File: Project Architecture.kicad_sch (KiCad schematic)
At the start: 0 parts

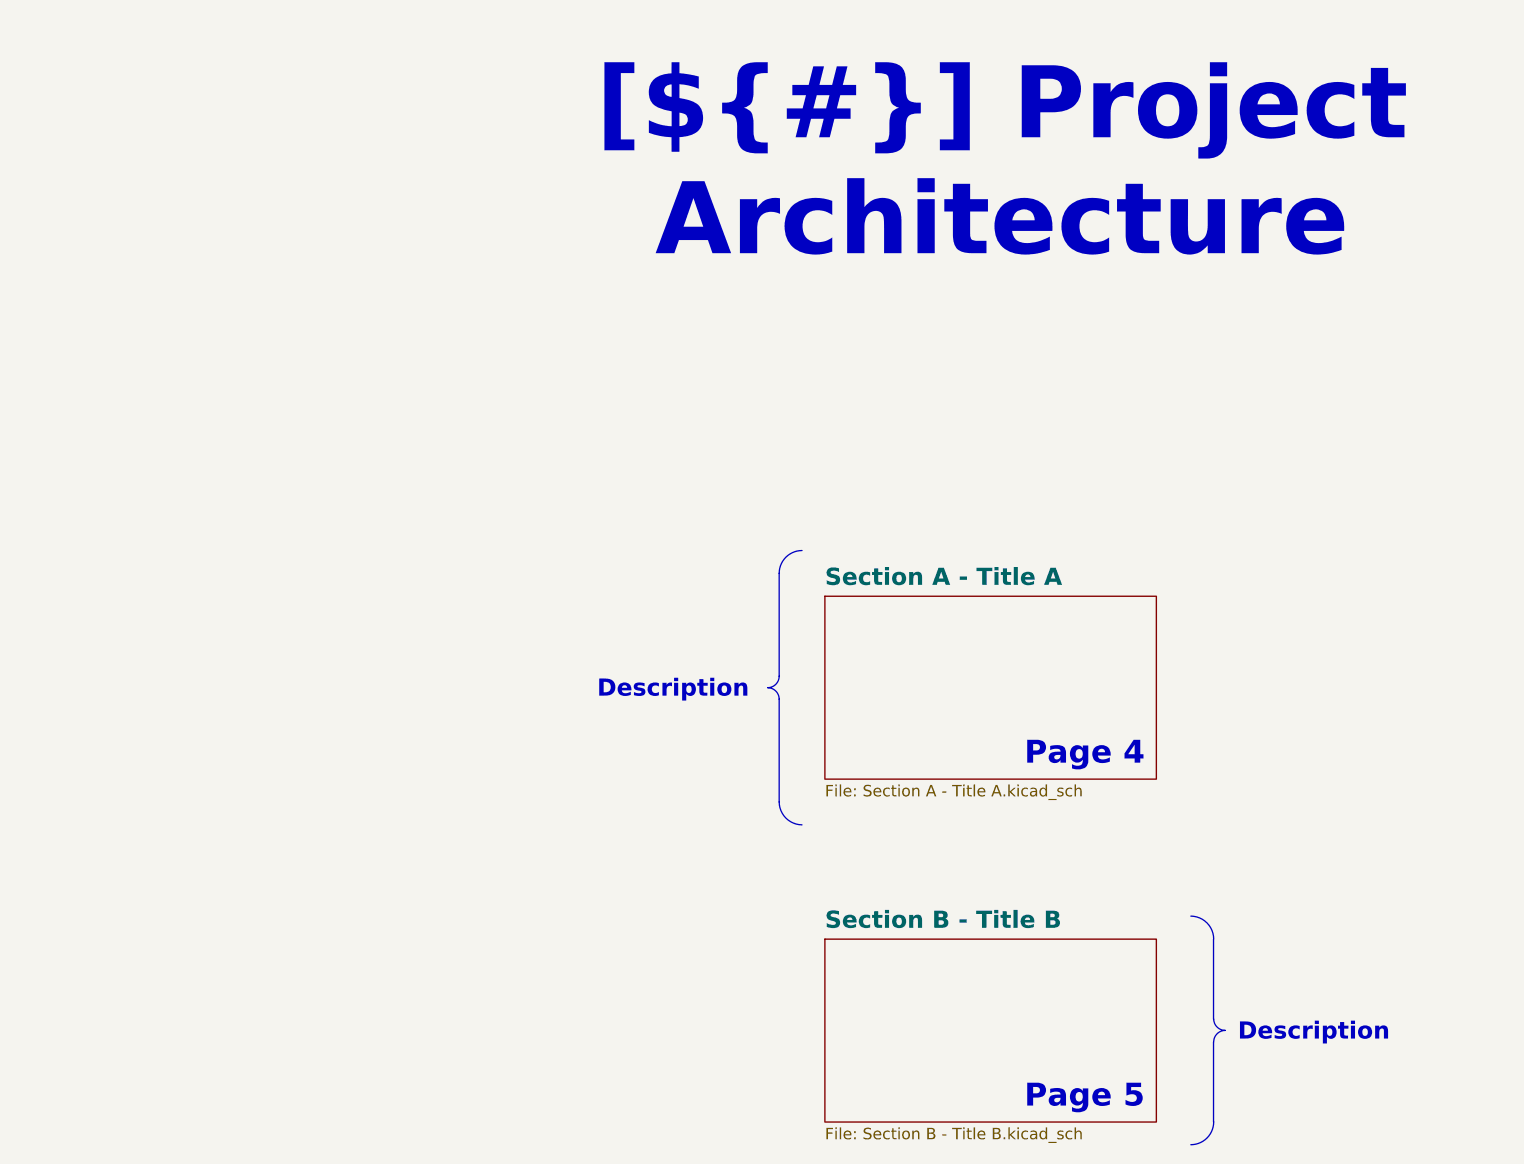
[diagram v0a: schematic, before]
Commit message: PCB[Layout and Routing]: Routing and layout done, changed to micofit connector, need to review and fix drc errors. SCH[Connector & Fuse]: Schmatic for connector, fuse and board to board layout, need to cleanup and add board standoffs.
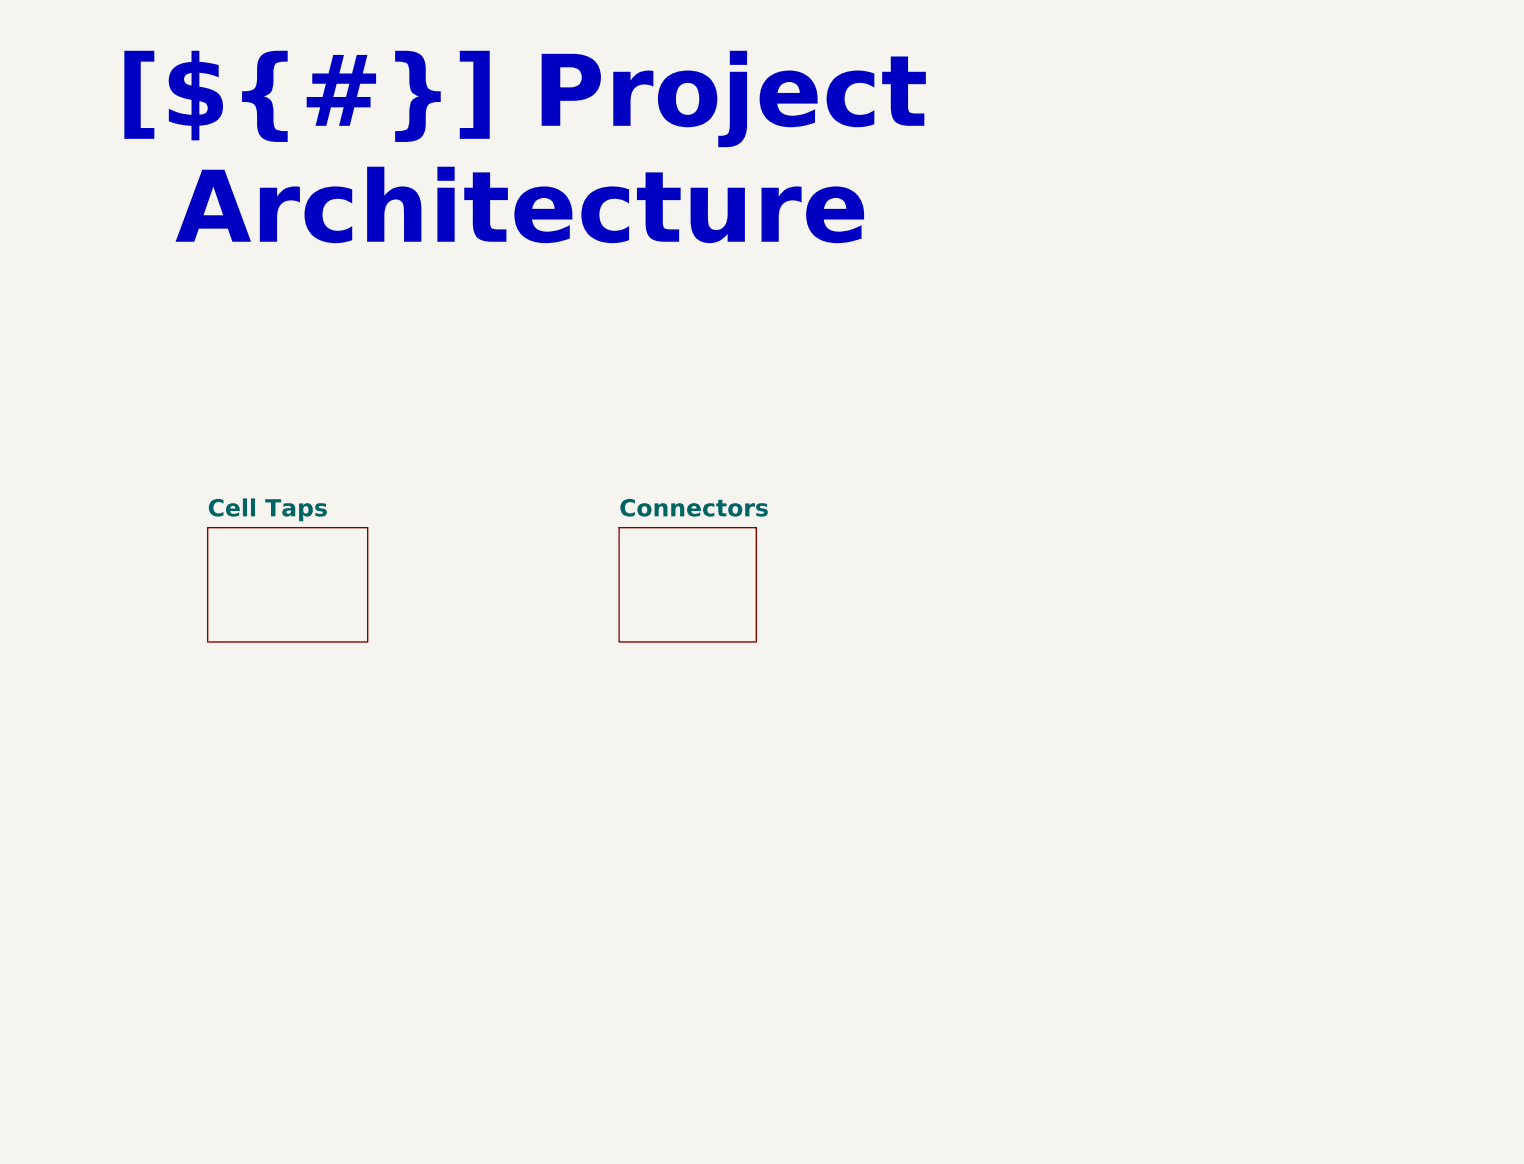
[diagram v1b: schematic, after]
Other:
- removed sheet Section A - Title A
- removed sheet Section B - Title B
- added sheet Cell Taps (celltaps.kicad_sch)
- added sheet Connectors (connectors.kicad_sch)
- note removed: "Page 4"
- note removed: "Page 5"

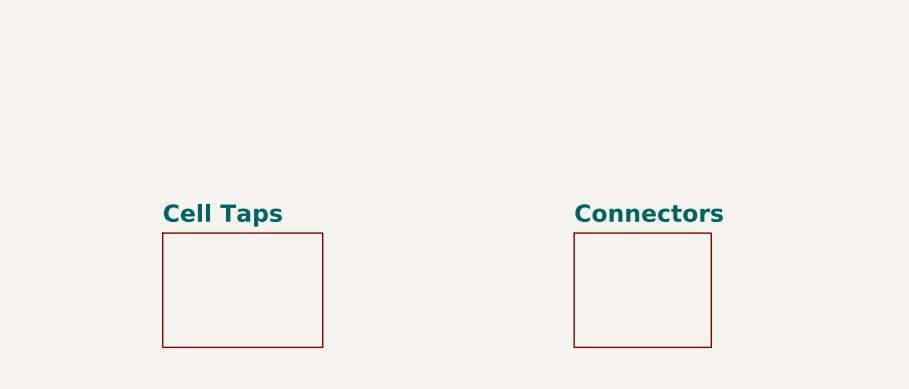
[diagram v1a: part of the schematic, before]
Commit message: PCB[Mounting]: Added standoffs going to test clearnaces. SCH[Mechanical]: Added standoffs, 14mm metal smt, small naming changes to match bms_slave sch.
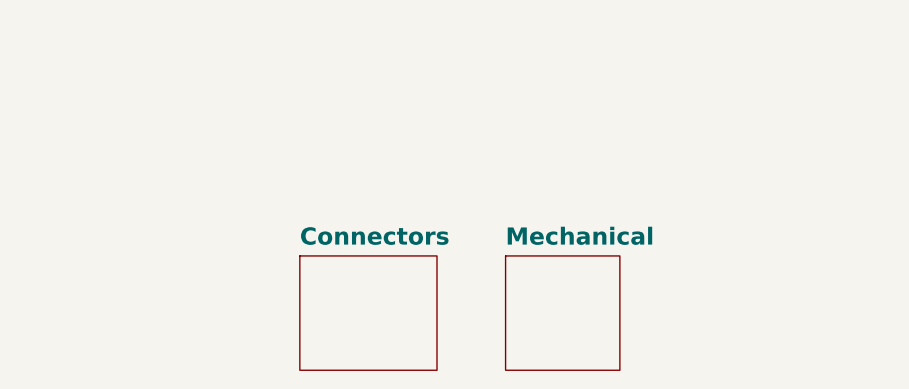
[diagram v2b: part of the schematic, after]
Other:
- removed sheet Cell Taps
- added sheet Mechanical (mechanical.kicad_sch)
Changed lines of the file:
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@@
 	(title_block
 		(title "Project Architecture")
-		(date "2026-10-12")
+		(date "2026-10-16")
 		(rev "${REVISION}")
 		(company "${COMPANY}")
@@
 	)
 	(sheet
-		(at 167.64 68.58)
+		(at 160.02 71.12)
+		(size 12.7 12.7)
+		(exclude_from_sim no)
+		(in_bom yes)
+		(on_board yes)
+		(dnp no)
+		(fields_autoplaced yes)
+		(stroke
+			(width 0.1524)
+			(type solid)
+		)
+		(fill
+			(color 0 0 0 0)
+		)
+		(property "Sheetname" "Mechanical"
+			(at 160.02 70.0909 0)
+			(show_name no)
+			(do_not_autoplace no)
+			(effects
+				(font
+					(size 1.905 1.905)
+					(thickness 0.381)
+					(bold yes)
+				)
+				(justify left bottom)
+			)
+		)
+		(property "Sheetfile" "mechanical.kicad_sch"
+			(at 160.02 84.4046 0)
+			(hide yes)
+			(show_name no)
+			(do_not_autoplace no)
+			(effects
+				(font
+					(size 1.27 1.27)
+				)
+				(justify left top)
+			)
+		)
+		(instances
+			(project "battery_interface_board"
+				(path "/f9e05184-c88b-4a88-ae9c-ab2bdb32be7c/c5103ceb-5325-4a84-a025-9638a412984e"
+					(page "5")
+				)
+			)
+		)
+	)
+	(sheet
+		(at 137.16 71.12)
 		(size 15.24 12.7)
 		(exclude_from_sim no)
@@
 		)
 		(property "Sheetname" "Connectors"
-			(at 167.64 67.5509 0)
+			(at 137.16 70.0909 0)
 			(show_name no)
 			(do_not_autoplace no)
@@
 		)
 		(property "Sheetfile" "connectors.kicad_sch"
-			(at 167.64 81.8646 0)
+			(at 137.16 84.4046 0)
 			(hide yes)
 			(show_name no)
@@
 				)
 			)
-		)
-	)
-	(sheet
-		(at 121.92 68.58)
-		(size 17.78 12.7)
-		(exclude_from_sim no)
-		(in_bom yes)
-		(on_board yes)
-		(dnp no)
-		(fields_autoplaced yes)
-		(stroke
-			(width 0.1524)
-			(type solid)
-		)
-		(fill
-			(color 0 0 0 0)
-		)
-		(property "Sheetname" "Cell Taps"
-			(at 121.92 67.5509 0)
-			(show_name no)
-			(do_not_autoplace no)
-			(effects
-				(font
-					(size 1.905 1.905)
-					(thickness 0.381)
-					(bold yes)
-				)
-				(justify left bottom)
-			)
-		)
-		(property "Sheetfile" "celltaps.kicad_sch"
-			(at 121.92 81.8646 0)
-			(hide yes)
-			(show_name no)
-			(do_not_autoplace no)
-			(effects
-				(font
-					(size 1.27 1.27)
-				)
-				(justify left top)
-			)
-		)
-		(instances
-			(project "battery_interface_board"
-				(path "/f9e05184-c88b-4a88-ae9c-ab2bdb32be7c/c5103ceb-5325-4a84-a025-9638a412984e"
-					(page "5")
-				)
-			)

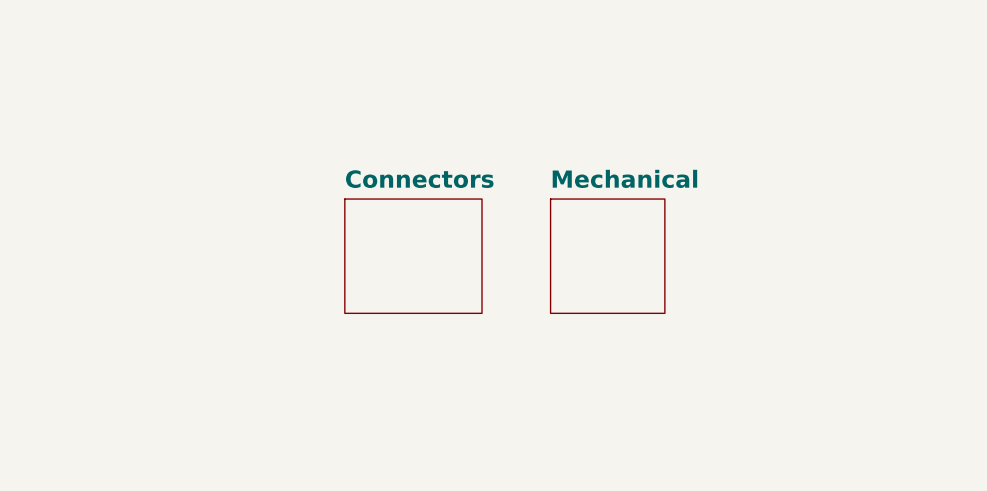
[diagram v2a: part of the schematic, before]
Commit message: SCH[Clean]: Cleaned up some schmatic errors.
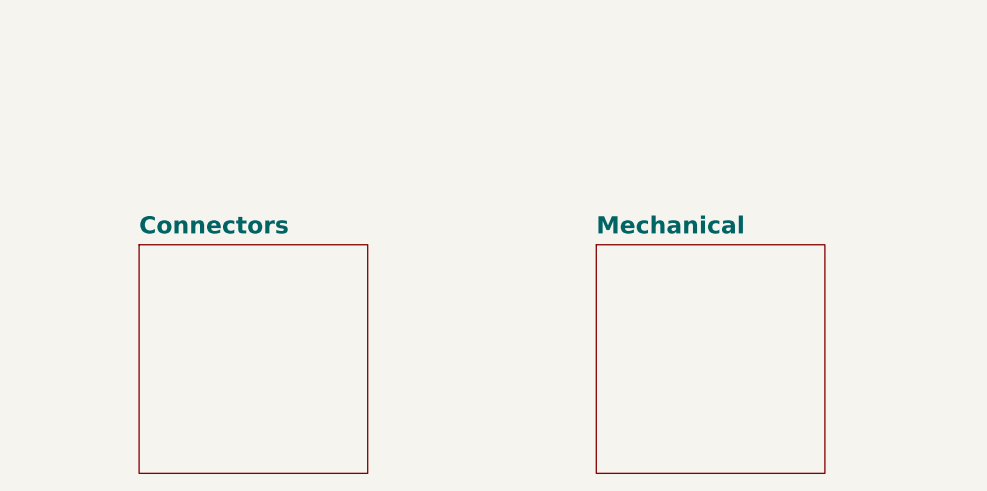
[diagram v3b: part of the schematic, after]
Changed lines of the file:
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@@
 	)
 	(sheet
-		(at 160.02 71.12)
-		(size 12.7 12.7)
+		(at 165.1 76.2)
+		(size 25.4 25.4)
 		(exclude_from_sim no)
 		(in_bom yes)
@@
 		(fields_autoplaced yes)
 		(stroke
-			(width 0.1524)
+			(width 0)
 			(type solid)
 		)
 		(fill
-			(color 0 0 0 0)
+			(color 255 255 194 1)
 		)
 		(property "Sheetname" "Mechanical"
-			(at 160.02 70.0909 0)
+			(at 165.1 75.1709 0)
 			(show_name no)
 			(do_not_autoplace no)
@@
 		)
 		(property "Sheetfile" "mechanical.kicad_sch"
-			(at 160.02 84.4046 0)
+			(at 165.1 102.1846 0)
 			(hide yes)
 			(show_name no)
@@
 	)
 	(sheet
-		(at 137.16 71.12)
-		(size 15.24 12.7)
+		(at 114.3 76.2)
+		(size 25.4 25.4)
 		(exclude_from_sim no)
 		(in_bom yes)
@@
 		(fields_autoplaced yes)
 		(stroke
-			(width 0.1524)
+			(width 0)
 			(type solid)
 		)
 		(fill
-			(color 0 0 0 0)
+			(color 255 255 194 1)
 		)
 		(property "Sheetname" "Connectors"
-			(at 137.16 70.0909 0)
+			(at 114.3 75.1709 0)
 			(show_name no)
 			(do_not_autoplace no)
@@
 		)
 		(property "Sheetfile" "connectors.kicad_sch"
-			(at 137.16 84.4046 0)
+			(at 114.3 102.1846 0)
 			(hide yes)
 			(show_name no)
